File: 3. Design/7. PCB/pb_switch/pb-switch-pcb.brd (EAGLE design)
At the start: 16.2 x 14.2 mm, 8 parts, among them Q1 2N7002NXAKR

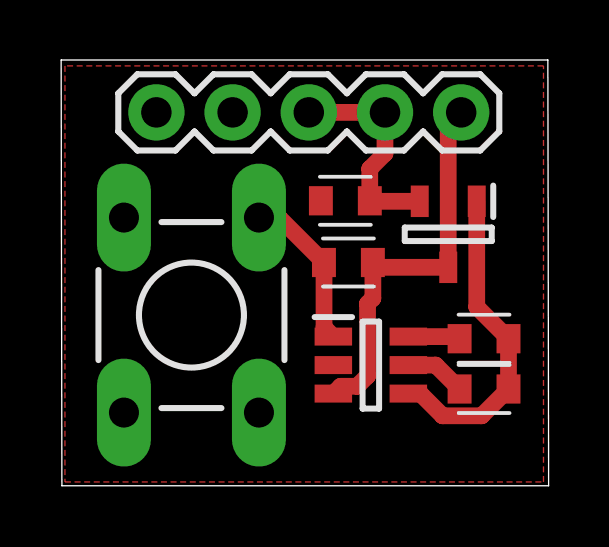
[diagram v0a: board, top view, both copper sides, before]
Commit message: ADD|UPDT: PB switch PCB 3D model
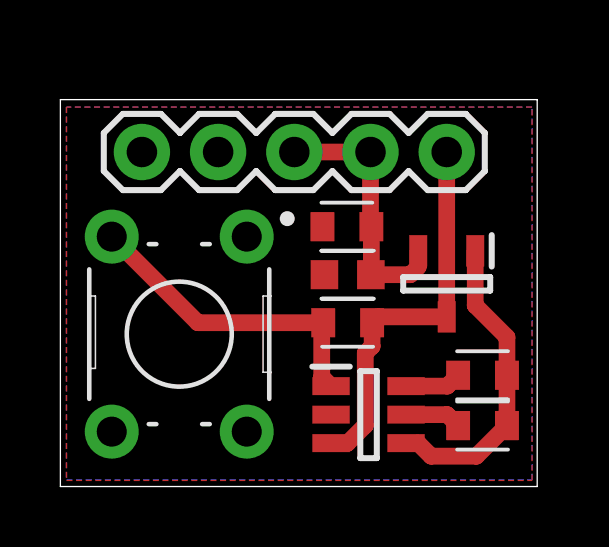
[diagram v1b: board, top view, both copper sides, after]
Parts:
- removed S1: DTS-6, switch-tact:DTS-6
- added C1: 100n [0603], Capacitor:CAPC1608X85
- added SW1: B3F-1000, Switch:B3F-1000
- R2: value 100k [0603] -> 1M [0603]
- moved R1 2.01 mm to (9.58, 5.46)
- moved PB_CTRL 1.65 mm to (10.3, 2.40)
- moved Q1 1.65 mm to (12.9, 6.76)
- moved J1 1.41 mm to (2.72, 11.2)
- moved R5 1.22 mm to (14.1, 2.03)
- moved R6 1.22 mm to (14.1, 3.71)
- moved R2 0.87 mm to (9.55, 8.66)
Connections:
- net GND: now also C1.2, SW1.1; no longer S1.2
- net N$2: now also SW1.3; no longer S1.4
- net VOUT: now also C1.1
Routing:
- net N$2: track 5.39 -> 10.5 mm
- net VOUT: track 7.37 -> 8.87 mm
- added copper zone on layer 16, net GND
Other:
- board size 16.2 x 14.2 mm -> 15.9 x 12.9 mm

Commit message: FIX: replaced load switching MOSFET with an actual load switch
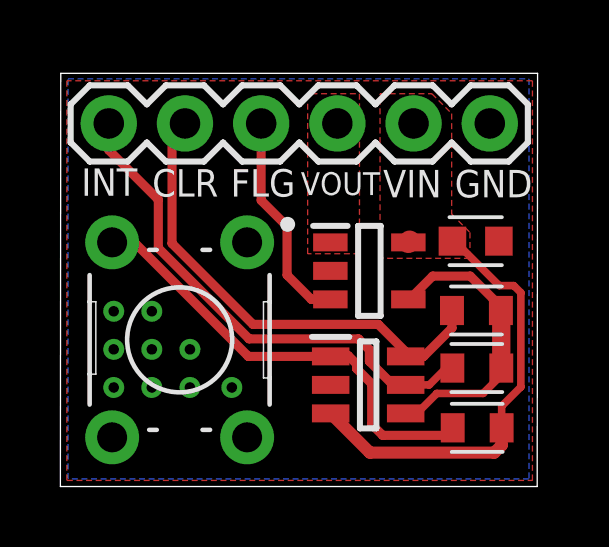
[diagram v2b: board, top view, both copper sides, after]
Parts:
- removed C1: 100n [0603], Capacitor:CAPC1608X85
- removed J1: (no value), SparkFun-Connectors:1X05
- removed Q1: 2N7002NXAKR, 2N7002NXAKR:SOT95P230X110-3N
- removed R2: 1M [0603], Resistor:RESC1608X60
- added C2: 100n [0603], Capacitor:CAPC1608X85
- added J2: (no value), SparkFun-Connectors:1X06
- added PS1: AP22814AW5-7, AP22814AW5-7:SOT95P285X130-5N
- moved R1 5.56 mm to (13.9, 1.96)
- moved R6 2.17 mm to (13.9, 5.87)
- moved R5 1.93 mm to (13.9, 3.95)
- moved PB_CTRL 0.99 mm to (10.3, 3.39)
- moved SW1 0.19 mm to (3.98, 4.89)
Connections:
- net N$2 renamed SW
- removed net N$5: PB_CTRL.4, Q1.1, R5.2, R6.2
- removed net PWR_CLR: PB_CTRL.6, R6.1
- removed net PWR_INT: PB_CTRL.5, R5.1
- new net CLR: J2.2, PB_CTRL.6, R6.1
- new net EN: PB_CTRL.4, PS1.4, R5.2, R6.2
- new net FLG: J2.3, PS1.3
- new net INT: J2.1, PB_CTRL.5, R5.1
- net GND: now also C2.2, J2.6, PS1.2; no longer C1.2, J1.1, J1.2, R2.1
- net VIN: now also C2.1, J2.5, PS1.5; no longer J1.5, Q1.3
- net VOUT: now also J2.4, PS1.1; no longer C1.1, J1.3, J1.4, Q1.2, R2.2
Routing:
- net INT: track 0.00 -> 17.0 mm
- net CLR: track 0.00 -> 16.2 mm
- net N$5: track 10.2 -> 0.00 mm
- net EN: track 0.00 -> 9.85 mm
- net VOUT: track 8.87 -> 0.00 mm
- net FLG: track 0.00 -> 7.19 mm
- net SW: track 10.5 -> 15.2 mm
- net PWR_INT: track 1.88 -> 0.00 mm
- net PWR_CLR: track 1.88 -> 0.00 mm
- net VIN: track 13.0 -> 14.7 mm
- added copper zone on layer 1, net VIN
- added copper zone on layer 1, net VOUT
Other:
- board size 15.9 x 12.9 mm -> 15.9 x 13.8 mm
- board text added: "CLR"
- board text added: "FLG"
- board text added: "GND"
- board text added: "INT"
- board text added: "VIN"
- board text added: "VOUT"

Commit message: UPDT: Added bypass capacitor at the output, enlarged power paths and optimized power
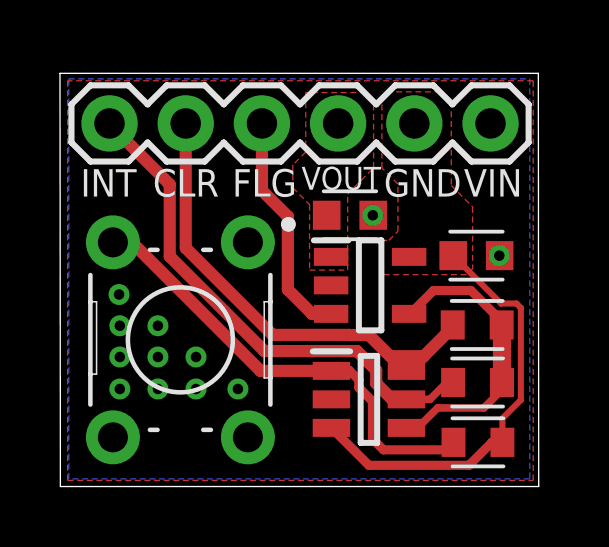
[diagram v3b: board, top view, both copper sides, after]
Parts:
- added C1: 100n [0603], Capacitor:CAPC1608X85
- moved PS1 0.48 mm to (10.3, 6.71)
- moved C2 0.48 mm to (13.9, 7.70)
- moved PB_CTRL 0.48 mm to (10.3, 2.90)
- moved R5 0.48 mm to (13.9, 3.47)
- moved R1 0.48 mm to (13.9, 1.47)
- moved R6 0.48 mm to (13.9, 5.38)
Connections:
- net GND: now also C1.2
- net VOUT: now also C1.1
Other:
- board size 15.9 x 13.8 mm -> 16 x 13.8 mm
